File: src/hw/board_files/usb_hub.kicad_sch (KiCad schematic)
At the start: 4 parts, among them J1 USB_C_Receptacle_USB2.0_14P, J2 USB_A, J3 Micro_SD_Card, U3 USB2514B_Bi

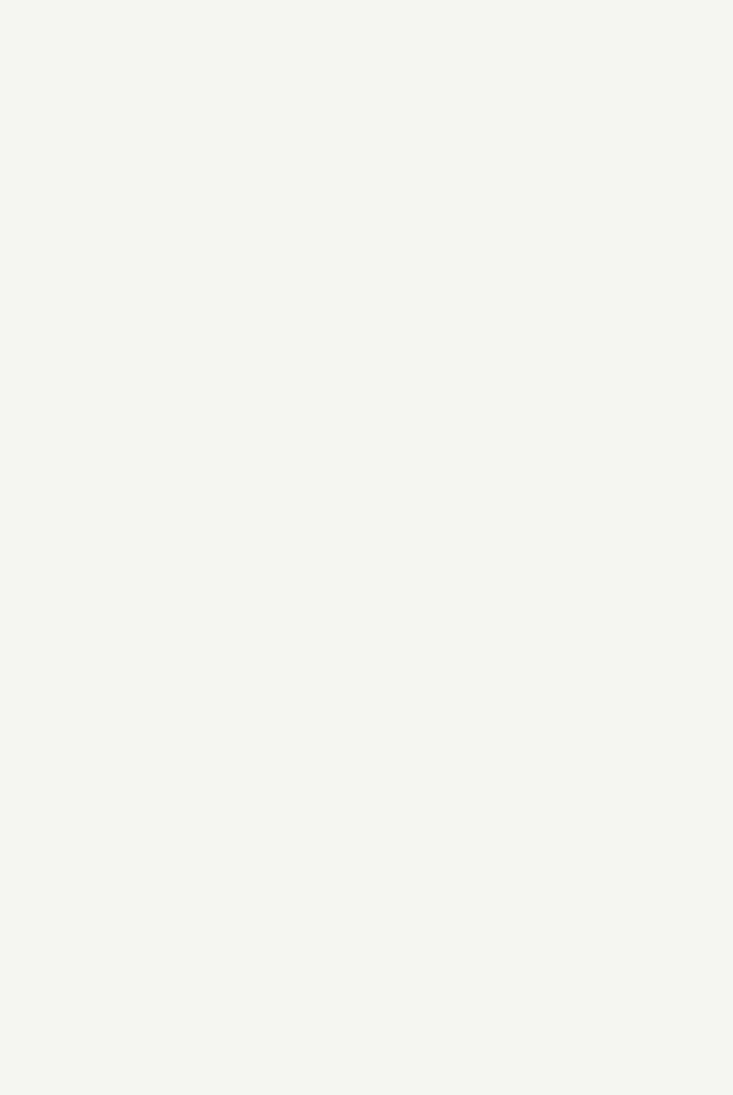
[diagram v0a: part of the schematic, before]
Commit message: Made USB hub symbol
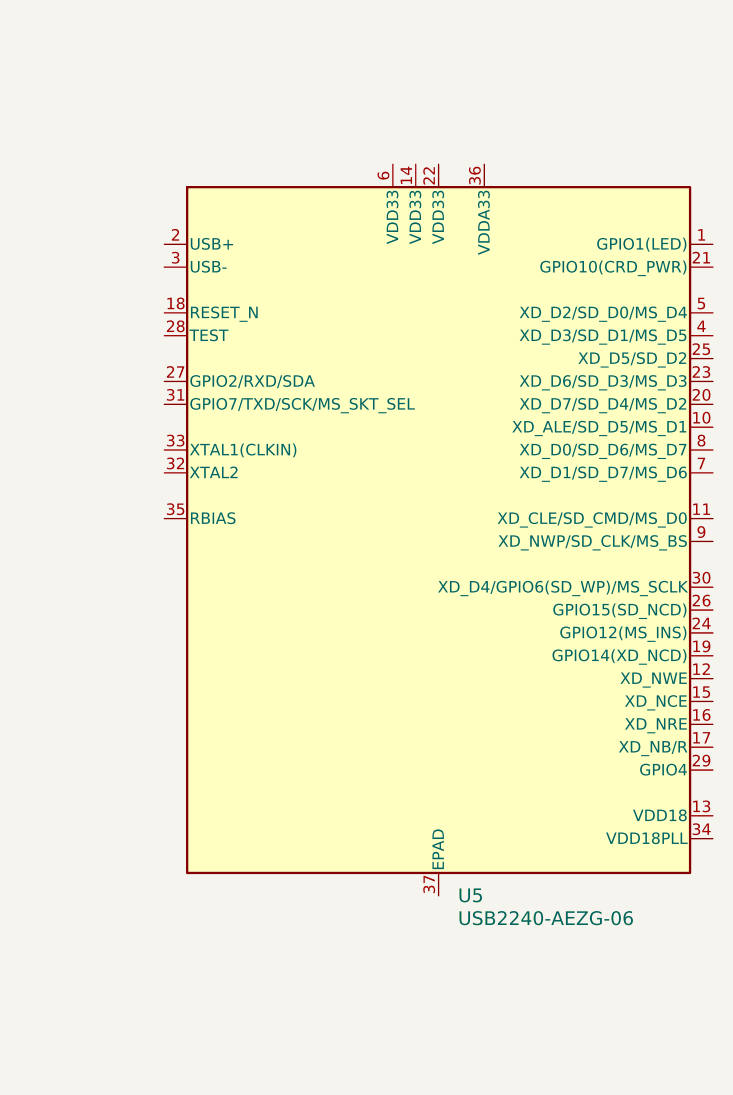
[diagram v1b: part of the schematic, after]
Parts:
- added U5: USB2240-AEZG-06, Package_DFN_QFN:QFN-36-1EP_6x6mm_P0.5mm_EP4.1x4.1mm_ThermalVias, symbol Project_Library:USB2240-AEZG-06
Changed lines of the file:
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@@
+	)
+	(symbol
+		(lib_id "Project_Library:USB2240-AEZG-06")
+		(at 231.14 91.44 0)
+		(unit 1)
+		(exclude_from_sim no)
+		(in_bom yes)
+		(on_board yes)
+		(dnp no)
+		(fields_autoplaced yes)
+		(property "Reference" "U5"
+			(at 233.2833 130.81 0)
+			(effects
+				(font
+					(size 1.524 1.524)
+				)
+				(justify left)
+			)
+		)
+		(property "Value" "USB2240-AEZG-06"
+			(at 233.2833 133.35 0)
+			(effects
+				(font
+					(size 1.524 1.524)
+				)
+				(justify left)
+			)
+		)
+		(property "Footprint" "Package_DFN_QFN:QFN-36-1EP_6x6mm_P0.5mm_EP4.1x4.1mm_ThermalVias"
+			(at 231.14 141.986 0)
+			(effects
+				(font
+					(size 1.27 1.27)
+					(italic yes)
+				)
+				(hide yes)
+			)
+		)
+		(property "Datasheet" "https://ww1.microchip.com/downloads/en/DeviceDoc/00001979A.pdf"
+			(at 231.14 144.272 0)
+			(effects
+				(font
+					(size 1.27 1.27)
+					(italic yes)
+				)
+				(hide yes)
+			)
+		)
+		(property "Description" "Desktop, Notebook PCs Interface 36-QFN (6x6)"
+			(at 231.14 146.558 0)
+			(effects
+				(font
+					(size 1.27 1.27)
+				)
+				(hide yes)
+			)
+		)
+		(pin "33"
+		)
+		(pin "12"
+		)
+		(pin "22"
+		)
+		(pin "14"
+		)
+		(pin "20"
+		)
+		(pin "16"
+		)
+		(pin "31"
+		)
+		(pin "21"
+		)
+		(pin "11"
+		)
+		(pin "13"
+		)
+		(pin "17"
+		)
+		(pin "18"
+		)
+		(pin "36"
+		)
+		(pin "35"
+		)
+		(pin "27"
+		)
+		(pin "29"
+		)
+		(pin "30"
+		)
+		(pin "26"
+		)
+		(pin "25"
+		)
+		(pin "23"
+		)
+		(pin "28"
+		)
+		(pin "37"
+		)
+		(pin "15"
+		)
+		(pin "34"
+		)
+		(pin "32"
+		)
+		(pin "24"
+		)
+		(pin "19"
+		)
+		(pin "8"
+		)
+		(pin "4"
+		)
+		(pin "3"
+		)
+		(pin "2"
+		)
+		(pin "1"
+		)
+		(pin "5"
+		)
+		(pin "6"
+		)
+		(pin "7"
+		)
+		(pin "9"
+		)
+		(pin "10"
+		)
+		(instances
+			(project ""
+				(path "/62136966-d911-451f-9518-a7827b282fe3/63faa32d-2c04-481a-ac3c-d2ba9de55eb3"
+					(reference "U5")
+					(unit 1)
+				)
+			)
+		)
 	)
 	(symbol
@@
 		)
 		(instances
-			(project ""
+			(project "keypad_usb_hub"
 				(path "/62136966-d911-451f-9518-a7827b282fe3/63faa32d-2c04-481a-ac3c-d2ba9de55eb3"
 					(reference "J3")
@@
 		)
 		(instances
-			(project ""
+			(project "keypad_usb_hub"
 				(path "/62136966-d911-451f-9518-a7827b282fe3/63faa32d-2c04-481a-ac3c-d2ba9de55eb3"
 					(reference "U3")

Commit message: Schematic progress
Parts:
- removed J2: USB_A, symbol Connector:USB_A
- removed J3: Micro_SD_Card, symbol Connector:Micro_SD_Card
- removed U5: USB2240-AEZG-06, Package_DFN_QFN:QFN-36-1EP_6x6mm_P0.5mm_EP4.1x4.1mm_ThermalVias, symbol Project_Library:USB2240-AEZG-06
- added C1, C10, C2, C5, C6, C7, C8, C9: 100n, symbol Device:C_Small
- added C11: 10u, symbol Device:C_Small
- added C3, C4: 18p, symbol Device:C_Small
- added FB1: FerriteBead_Small, symbol Device:FerriteBead_Small
- added R1: 12k, symbol Device:R_Small_US
- added R15, R16: 10k, symbol Device:R_Small_US
- added R3, R4: 5k1, symbol Device:R_Small_US
- added R5, R6, R7, R8: 100k, symbol Device:R_Small_US
- added U6: TPS2042D, Package_SO:SOIC-8_3.9x4.9mm_P1.27mm, symbol Power_Management:TPS2042D
- added Y1: 24MHz, symbol Device:Crystal_Small
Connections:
- net MCU_USB_D-: now reaches U3.1 (USBDM_DN1/PRT_DIS_M1)
- net +3V3: now reaches U3.10 (VDDA33)
- net +3V3: now also U3.29 (VDDA33), U3.36 (VDDA33), U3.5 (VDDA33), C5.2, C6.2, C7.2, C8.2, FB1.2, R15.2, R16.2, R8.1
- net at U3.14 (CRFILT): now also C1.2
- net at U3.15 (VDD33): now also U3.23 (VDD33), C10.2, C11.2, C9.2, FB1.1
- net at U3.18 (PRTPWR3/BC_EN3): now also U6.3 (~{EN1})
- net at U3.19 (OCS_N3): now also R15.1, U6.8 (~{OC1})
- net MCU_USB_D+: now reaches U3.2 (USBDP_DN1/PRT_DIS_P1)
- net at U3.20 (PRTPWR4/BC_EN4): now also U6.4 (~{EN2})
- net at U3.21 (OCS_N4): now also R16.1, U6.5 (~{OC2})
- net at U3.22 (SDA/SMBDATA/NON_REM1): now also R7.2
- net GND: now reaches U3.24 (SCL/SMBCLK/CFG_SEL0)
- net GND: now also J1.A1 (GND), J1.A12 (GND), J1.B1 (GND), J1.B12 (GND), J1.S1 (SHIELD), U3.25 (HS_IND/CFG_SEL1), U3.28 (SUSP_IND/LOCAL_PWR/NON_REM0), U3.37 (VSS), C1.1, C10.1, C11.1, C2.1, C3.1, C4.1, C5.1, C6.1, C7.1, C8.1, C9.1, R1.1, R3.1, R4.1, R6.1, R7.1, U6.1 (GND)
- net at U3.26 (RESET_N): now also R8.2
- net at U3.27 (VBUS_DET): now also R5.1, R6.2
- net SD_USB_D-: now reaches U3.3 (USBDM_DN2/PRT_DIS_M2)
- net USBC_D-: now reaches U3.30 (USBDM_UP)
- net USBC_D-: now also J1.A7 (D-), J1.B7 (D-)
- net USBC_D+: now reaches U3.31 (USBDP_UP)
- net USBC_D+: now also J1.A6 (D+), J1.B6 (D+)
- net at U3.32 (XTALOUT): now also C4.2, Y1.2
- net at U3.33 (XTALIN/CLKIN): now also C3.2, Y1.1
- net at U3.34 (PLLFILT): now also C2.2
- net at U3.35 (RBIAS): now also R1.2
- net SD_USB_D+: now reaches U3.4 (USBDP_DN2/PRT_DIS_P2)
- net USBC_PORT_D-: now reaches U3.6 (USBDM_DN3/PRT_DIS_M3)
- net USBC_PORT_D+: now reaches U3.7 (USBDP_DN3/PRT_DIS_P3)
- net USBA_PORT_D-: now reaches U3.8 (USBDM_DN4/PRT_DIS_M4)
- net USBA_PORT_D+: now reaches U3.9 (USBDP_DN4/PRT_DIS_P4)
- net VBUS_IN: now reaches J1.A4 (VBUS), J1.A9 (VBUS), J1.B4 (VBUS), J1.B9 (VBUS)
- net VBUS_IN: now also R5.2, U6.2 (IN1)
- net at J1.A5 (CC1): now also R4.2
- net at J1.B5 (CC2): now also R3.2
- new net VBUS_PORT3: U6.7 (OUT1)
- new net VBUS_PORT4: U6.6 (OUT2)
- no-connect marks 0 -> 5
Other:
- note added: "1% tol."
- note added: "USB Hub Controller"
- moved on the sheet: J1, U3

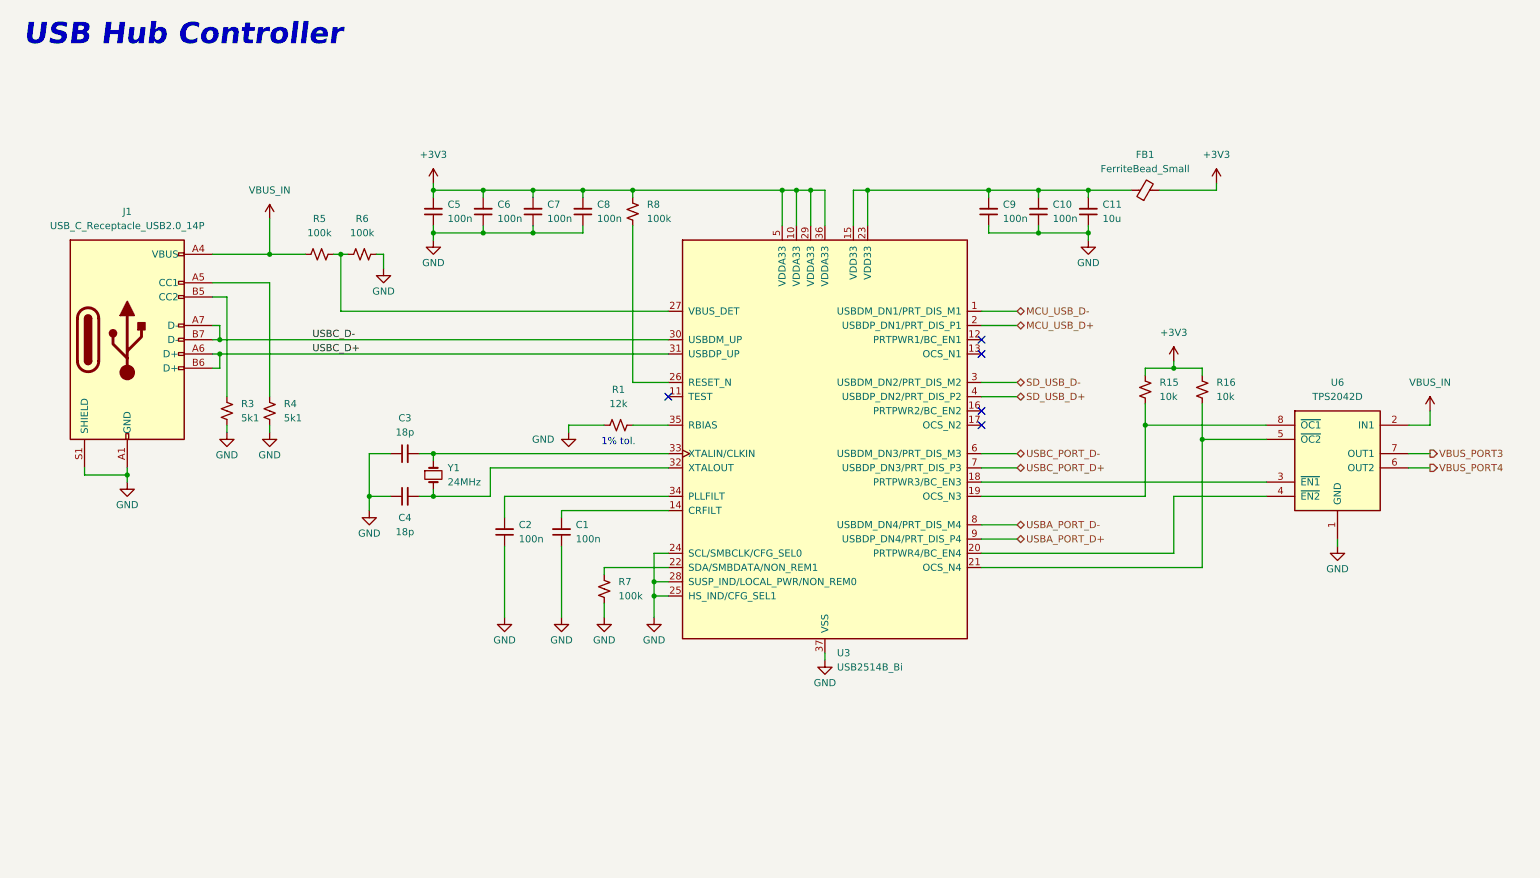
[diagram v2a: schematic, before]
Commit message: Finishing schematic. Need to review and clean up
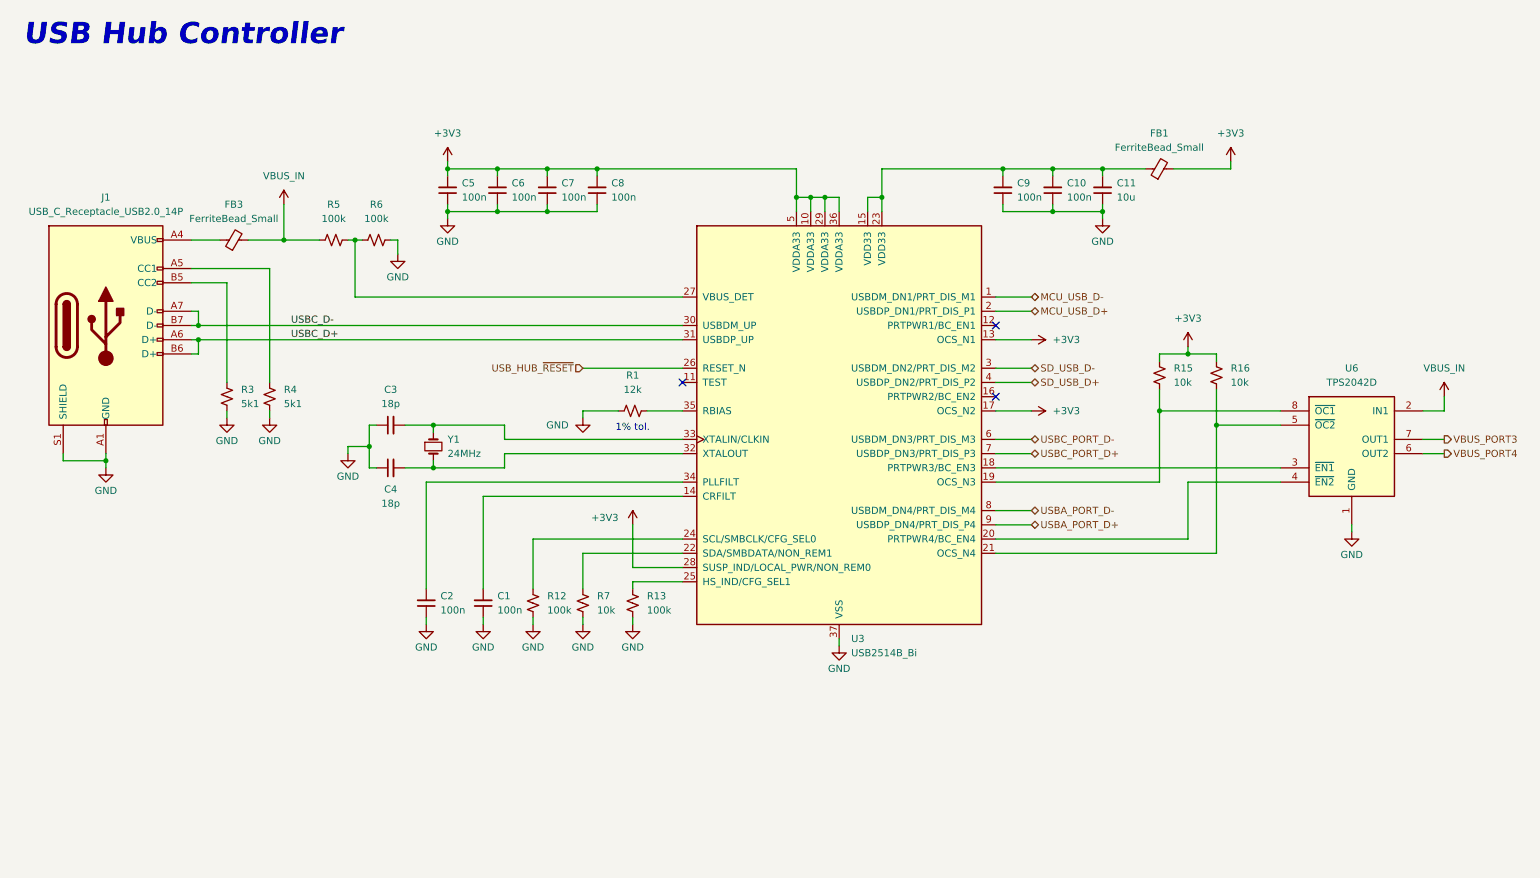
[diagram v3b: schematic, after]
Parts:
- removed R8: 100k, symbol Device:R_Small_US
- added FB3: FerriteBead_Small, symbol Device:FerriteBead_Small
- added R12, R13: 100k, symbol Device:R_Small_US
- R7: value 100k -> 10k
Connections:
- net +3V3: now also U3.13 (OCS_N1), U3.17 (OCS_N2), U3.28 (SUSP_IND/LOCAL_PWR/NON_REM0)
- net GND: now also R12.1, R13.1; no longer U3.24 (SCL/SMBCLK/CFG_SEL0), U3.25 (HS_IND/CFG_SEL1), U3.28 (SUSP_IND/LOCAL_PWR/NON_REM0)
- net VBUS_IN: now also FB3.2; no longer J1.A4 (VBUS), J1.A9 (VBUS), J1.B4 (VBUS), J1.B9 (VBUS)
- net USB_HUB_~{RESET}: now reaches U3.26 (RESET_N)
- new net: R12.2, U3.24 (SCL/SMBCLK/CFG_SEL0)
- new net: R13.2, U3.25 (HS_IND/CFG_SEL1)
- new net: FB3.1, J1.A4 (VBUS), J1.A9 (VBUS), J1.B4 (VBUS), J1.B9 (VBUS)
- no-connect marks 5 -> 3
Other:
- moved on the sheet: C1, C10, C11, C2, C3, C4, C5, C6, C7, C8, C9, FB1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

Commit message: Added all footprints, need to connect switches to MCU
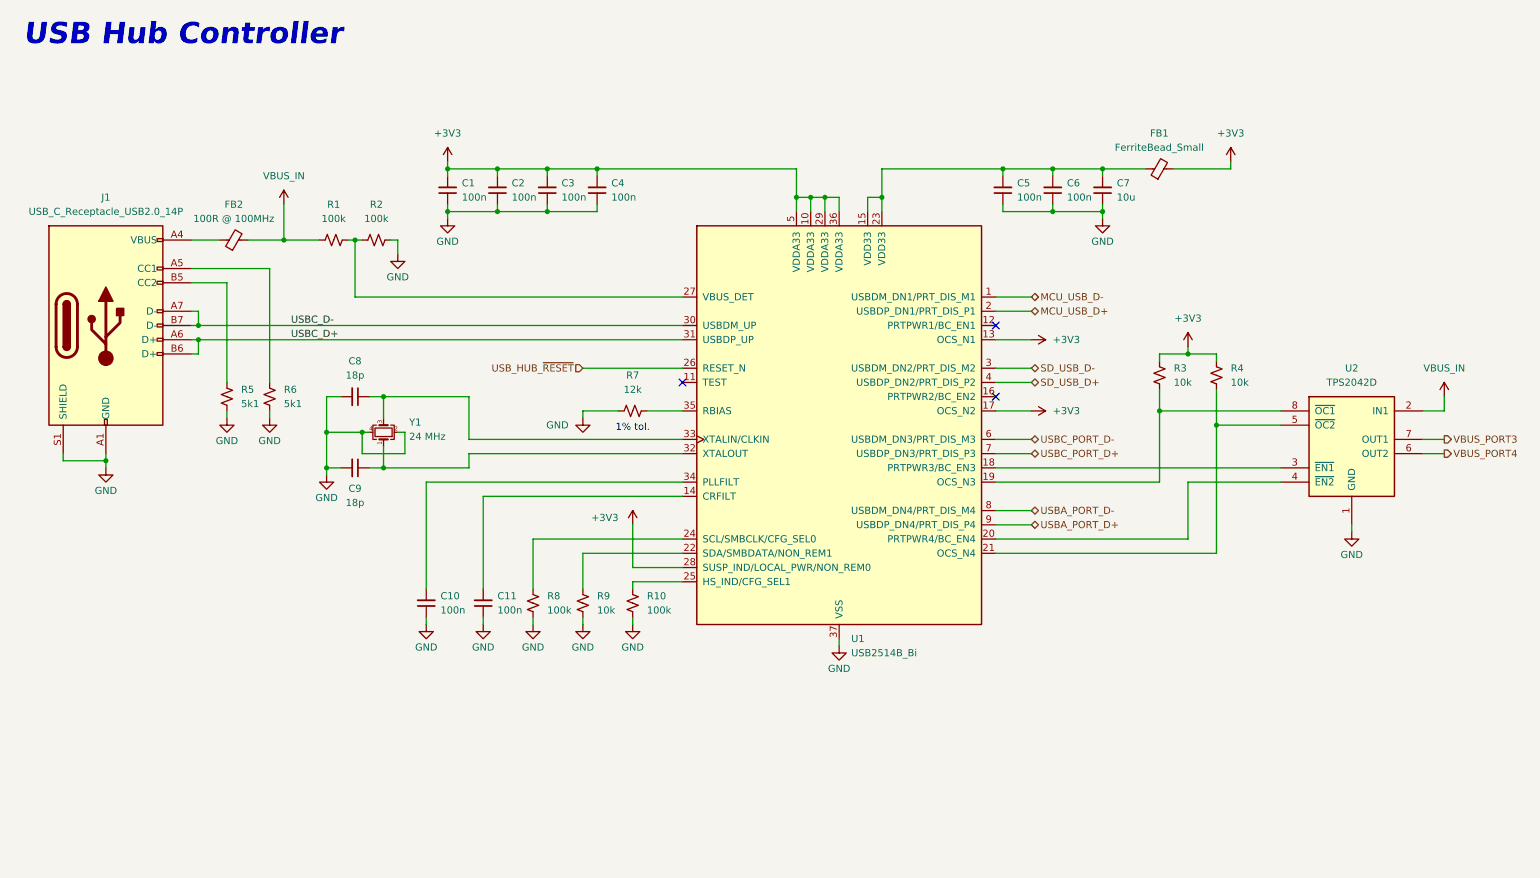
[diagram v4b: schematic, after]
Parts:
- removed C3, C4: 18p, symbol Device:C_Small
- removed Y1: 24MHz, symbol Device:Crystal_Small
- added C8, C9: 18p, Capacitor_SMD:C_0603_1608Metric_Pad1.08x0.95mm_HandSolder, symbol Device:C_Small
- added Y1: 24 MHz, Crystal:Crystal_SMD_Abracon_ABM8G-4Pin_3.2x2.5mm, symbol Device:Crystal_GND24_Small
- C1: renamed from C5; footprint (none) -> Capacitor_SMD:C_0603_1608Metric_Pad1.08x0.95mm_HandSolder
- C10: renamed from C2; footprint (none) -> Capacitor_SMD:C_0603_1608Metric_Pad1.08x0.95mm_HandSolder
- C11: renamed from C1; footprint (none) -> Capacitor_SMD:C_0603_1608Metric_Pad1.08x0.95mm_HandSolder
- C2: renamed from C6; footprint (none) -> Capacitor_SMD:C_0603_1608Metric_Pad1.08x0.95mm_HandSolder
- C3: renamed from C7; footprint (none) -> Capacitor_SMD:C_0603_1608Metric_Pad1.08x0.95mm_HandSolder
- C4: renamed from C8; footprint (none) -> Capacitor_SMD:C_0603_1608Metric_Pad1.08x0.95mm_HandSolder
- C5: renamed from C9; footprint (none) -> Capacitor_SMD:C_0603_1608Metric_Pad1.08x0.95mm_HandSolder
- C6: renamed from C10; footprint (none) -> Capacitor_SMD:C_0603_1608Metric_Pad1.08x0.95mm_HandSolder
- C7: renamed from C11; footprint (none) -> Capacitor_SMD:C_0805_2012Metric_Pad1.18x1.45mm_HandSolder
- FB1: footprint (none) -> Inductor_SMD:L_0603_1608Metric_Pad1.05x0.95mm_HandSolder
- FB2: renamed from FB3; value FerriteBead_Small -> 100R @ 100MHz; footprint (none) -> Inductor_SMD:L_0805_2012Metric_Pad1.15x1.40mm_HandSolder
- R1: renamed from R5; footprint (none) -> Resistor_SMD:R_0603_1608Metric_Pad0.98x0.95mm_HandSolder
- R10: renamed from R13; footprint (none) -> Resistor_SMD:R_0603_1608Metric_Pad0.98x0.95mm_HandSolder
- R2: renamed from R6; footprint (none) -> Resistor_SMD:R_0603_1608Metric_Pad0.98x0.95mm_HandSolder
- R3: renamed from R15; footprint (none) -> Resistor_SMD:R_0805_2012Metric_Pad1.20x1.40mm_HandSolder
- R4: renamed from R16; footprint (none) -> Resistor_SMD:R_0805_2012Metric_Pad1.20x1.40mm_HandSolder
- R5: renamed from R3; footprint (none) -> Resistor_SMD:R_0805_2012Metric_Pad1.20x1.40mm_HandSolder
- R6: renamed from R4; footprint (none) -> Resistor_SMD:R_0805_2012Metric_Pad1.20x1.40mm_HandSolder
- R7: renamed from R1; footprint (none) -> Resistor_SMD:R_0805_2012Metric_Pad1.20x1.40mm_HandSolder
- R8: renamed from R12; footprint (none) -> Resistor_SMD:R_0603_1608Metric_Pad0.98x0.95mm_HandSolder
- R9: renamed from R7; footprint (none) -> Resistor_SMD:R_0805_2012Metric_Pad1.20x1.40mm_HandSolder
- renumbered U3 to U1, U6 to U2
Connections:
- net GND: now also C8.2, C9.2, Y1.2, Y1.4
- net at U1.33 (XTALIN/CLKIN): now also C8.1, Y1.3
- net at U1.32 (XTALOUT): now also C9.1, Y1.1
